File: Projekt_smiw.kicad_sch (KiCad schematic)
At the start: 20 parts, among them J1 PWR 5V, J3 JTAG, J4 USB_C_Receptacle_USB2.0, SW1 SW_Omron_B3FS, SW2 SW_Omron_B3FS, U1 ESP32-S3-PICO-1, U2 NCP1117-2.85_TO252

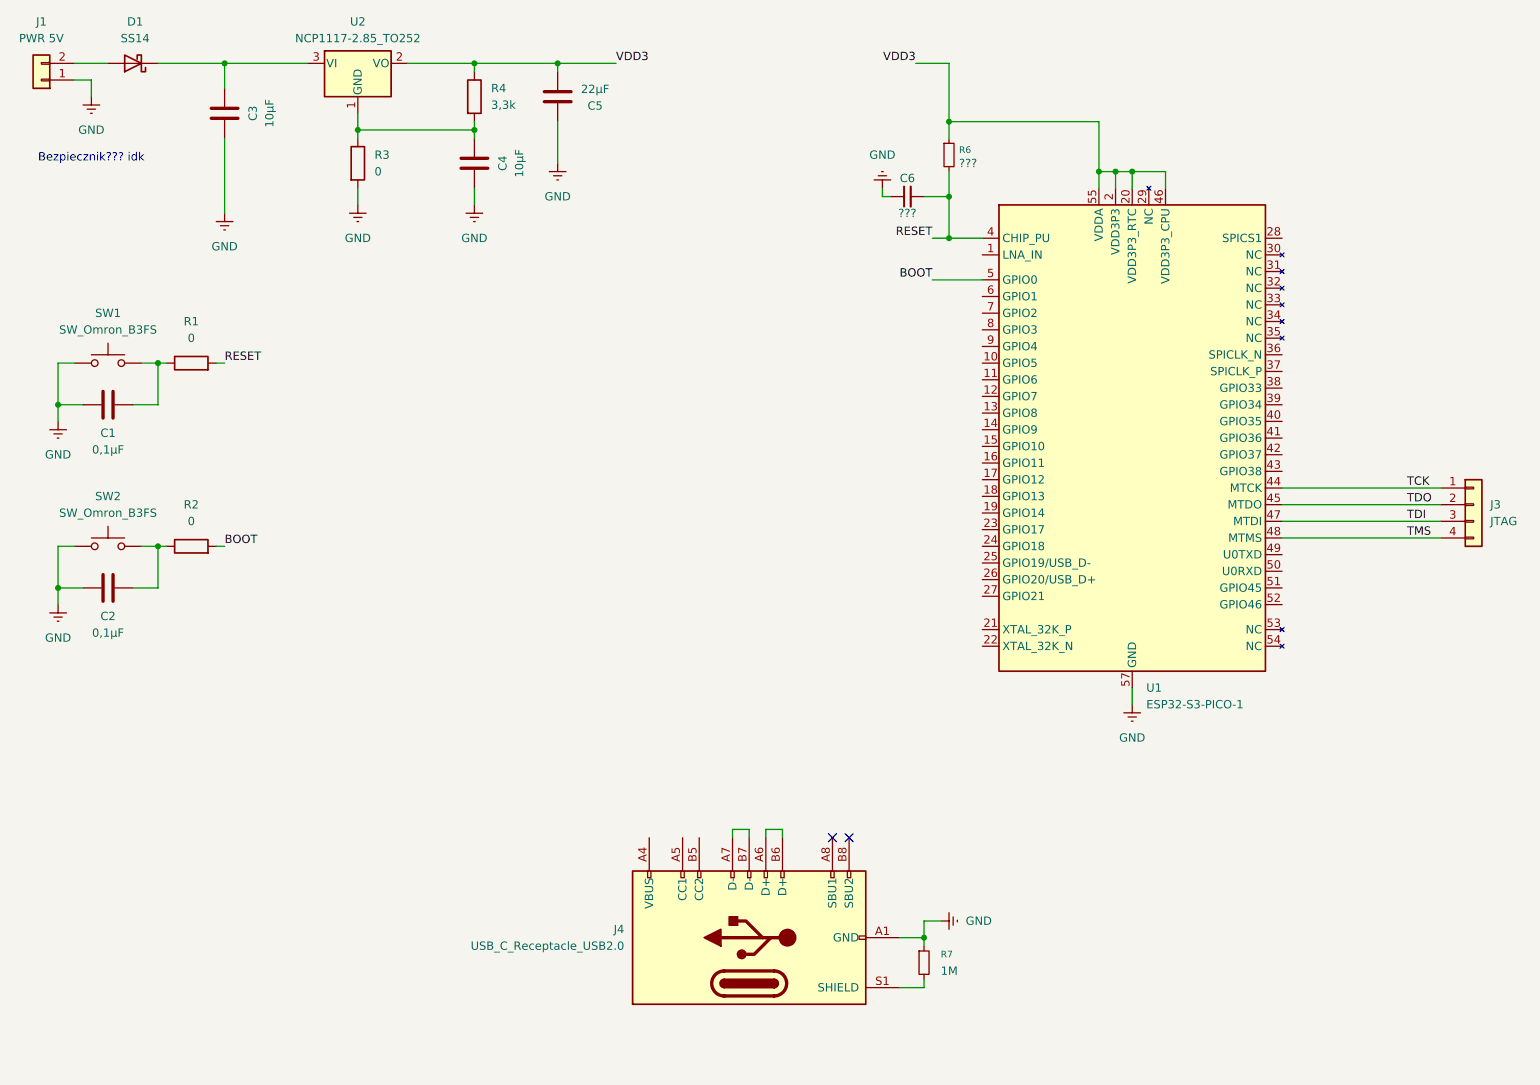
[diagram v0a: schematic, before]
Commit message: Pinout dla ESP32
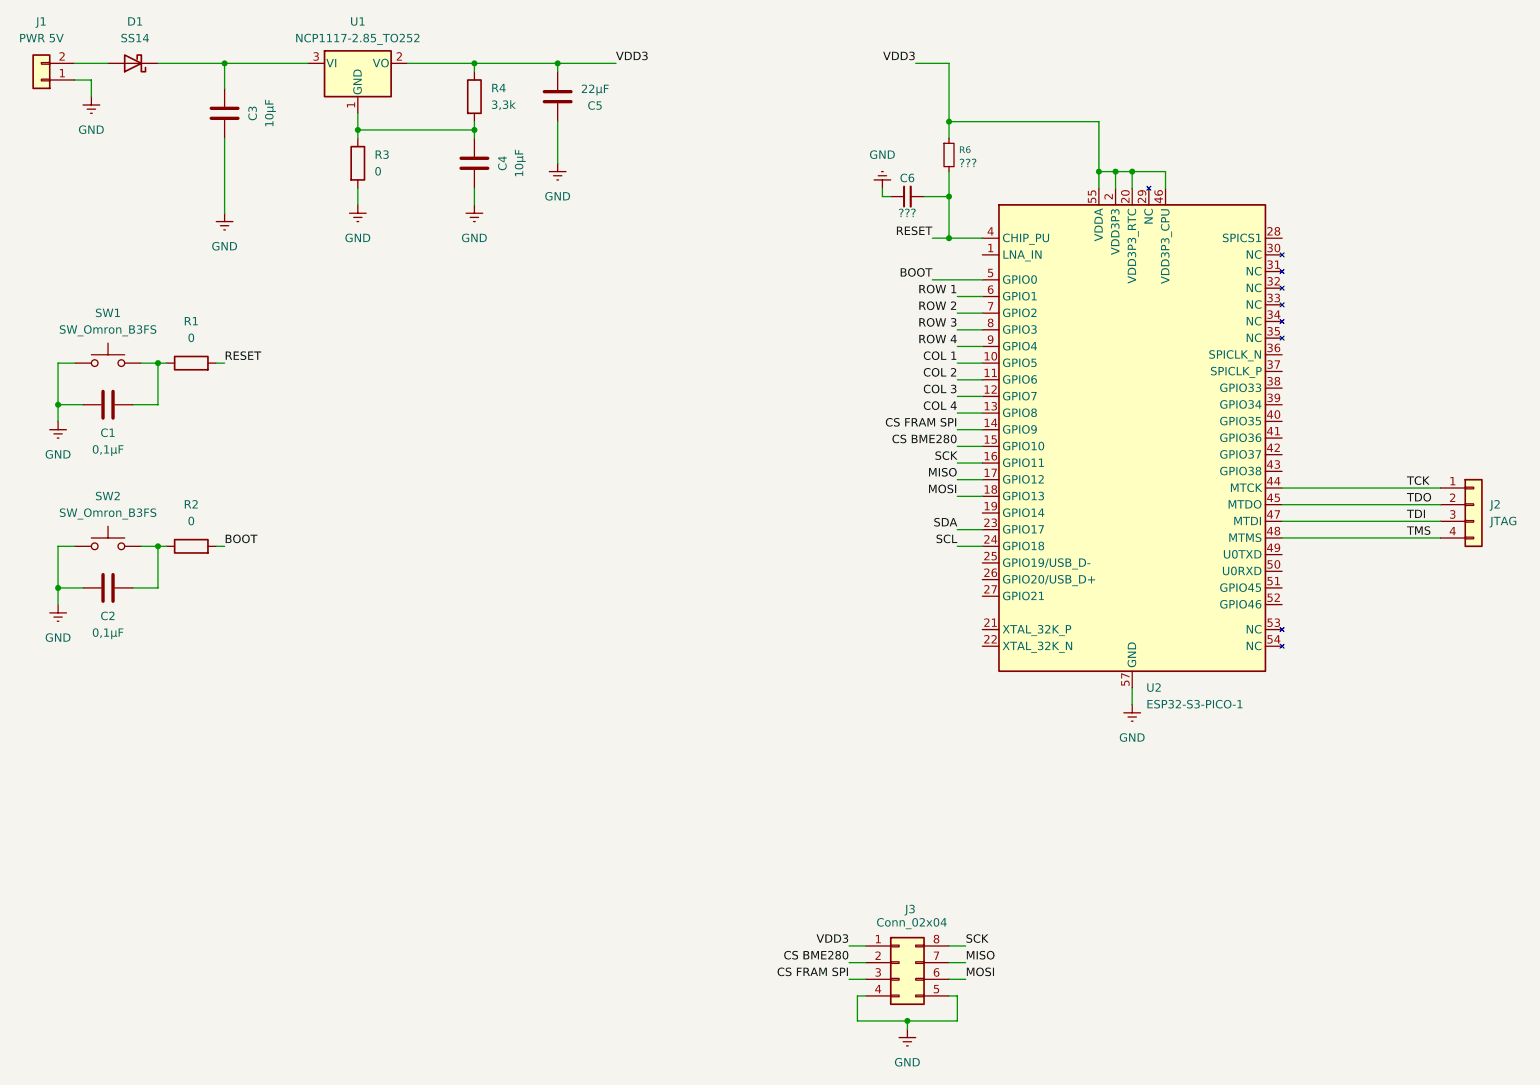
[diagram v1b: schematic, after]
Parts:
- removed J4: USB_C_Receptacle_USB2.0, symbol Connector:USB_C_Receptacle_USB2.0
- removed R7: 1M, symbol Device:R_Small
- added J3: Conn_02x04, symbol Connector_Generic:Conn_02x04_Counter_Clockwise
- SW1, SW2: footprint (none) -> Button_Switch_SMD:SW_SPST_Omron_B3FS-100xP
- renumbered J3 to J2, U2 to U1, U1 to U2
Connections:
- net GND: now also J3.4 (Pin_4), J3.5 (Pin_5)
- net VDD3: now also J3.1 (Pin_1)
- net COL 1: now reaches U2.10 (GPIO5)
- net COL 2: now reaches U2.11 (GPIO6)
- net COL 3: now reaches U2.12 (GPIO7)
- net COL 4: now reaches U2.13 (GPIO8)
- net CS FRAM SPI: now reaches U2.14 (GPIO9)
- net CS FRAM SPI: now also J3.3 (Pin_3)
- net CS BME280: now reaches U2.15 (GPIO10)
- net CS BME280: now also J3.2 (Pin_2)
- net SCK: now reaches U2.16 (GPIO11)
- net SCK: now also J3.8 (Pin_8)
- net MISO: now reaches U2.17 (GPIO12)
- net MISO: now also J3.7 (Pin_7)
- net MOSI: now reaches U2.18 (GPIO13)
- net MOSI: now also J3.6 (Pin_6)
- net SDA: now reaches U2.23 (GPIO17)
- net SCL: now reaches U2.24 (GPIO18)
- net ROW 1: now reaches U2.6 (GPIO1)
- net ROW 2: now reaches U2.7 (GPIO2)
- net ROW 3: now reaches U2.8 (GPIO3)
- net ROW 4: now reaches U2.9 (GPIO4)
- no-connect marks 2 -> 0
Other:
- note removed: "Bezpiecznik??? idk"

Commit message: wyswietlacz 1
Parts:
- added J4: Conn_K, symbol Connector_Generic:Conn_02x04_Counter_Clockwise
- added J5: Conn_W, symbol Connector_Generic:Conn_02x02_Counter_Clockwise
- J3: value Conn_02x04 -> Conn_C
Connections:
- net COL 1: now also J4.8 (Pin_8)
- net COL 2: now also J4.7 (Pin_7)
- net COL 3: now also J4.6 (Pin_6)
- net COL 4: now also J4.5 (Pin_5)
- net GND: now also J5.3 (Pin_3)
- net ROW 1: now also J4.1 (Pin_1)
- net ROW 2: now also J4.2 (Pin_2)
- net ROW 3: now also J4.3 (Pin_3)
- net ROW 4: now also J4.4 (Pin_4)
- net SCL: now also J5.4 (Pin_4)
- net SDA: now also J5.2 (Pin_2)
- net VDD3: now also J5.1 (Pin_1)

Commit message: Orange 21.37
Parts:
- removed J3: Conn_C, symbol Connector_Generic:Conn_02x04_Counter_Clockwise
- removed J4: Conn_K, symbol Connector_Generic:Conn_02x04_Counter_Clockwise
- removed J5: Conn_W, symbol Connector_Generic:Conn_02x02_Counter_Clockwise
- added J3: Conn, symbol Connector_Generic:Conn_02x09_Odd_Even
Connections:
- net COL 1: now also J3.2 (Pin_2)
- net COL 2: now also J3.4 (Pin_4)
- net COL 3: now also J3.6 (Pin_6)
- net COL 4: now also J3.8 (Pin_8)
- net CS BME280: now also J3.3 (Pin_3)
- net CS FRAM SPI: now also J3.5 (Pin_5)
- net GND: now also J3.17 (Pin_17), J3.18 (Pin_18)
- net MISO: now also J3.9 (Pin_9)
- net MOSI: now also J3.7 (Pin_7)
- net ROW 1: now also J3.16 (Pin_16)
- net ROW 2: now also J3.14 (Pin_14)
- net ROW 3: now also J3.12 (Pin_12)
- net ROW 4: now also J3.10 (Pin_10)
- net SCK: now also J3.11 (Pin_11)
- net SCL: now also J3.15 (Pin_15)
- net SDA: now also J3.13 (Pin_13)
- net VDD3: now also J3.1 (Pin_1)
